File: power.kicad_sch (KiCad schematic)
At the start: 29 parts, among them CN104 Power, IC109 L7805, SW101 SW_SPDT

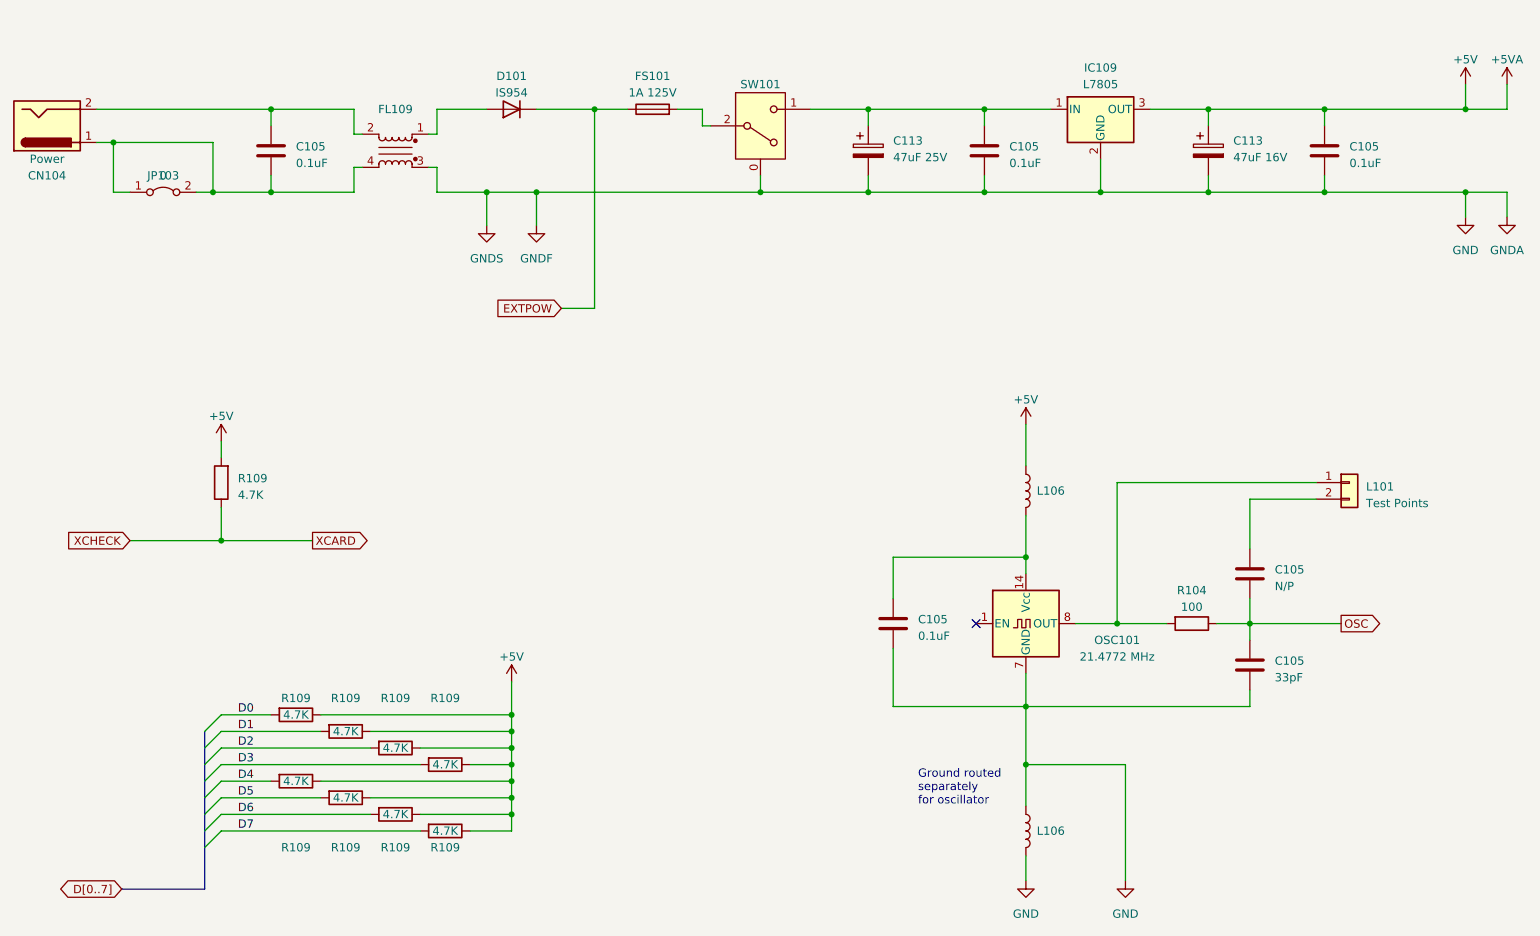
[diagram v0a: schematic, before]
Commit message: Inductor symbol for L101, schematic layout clean-up.
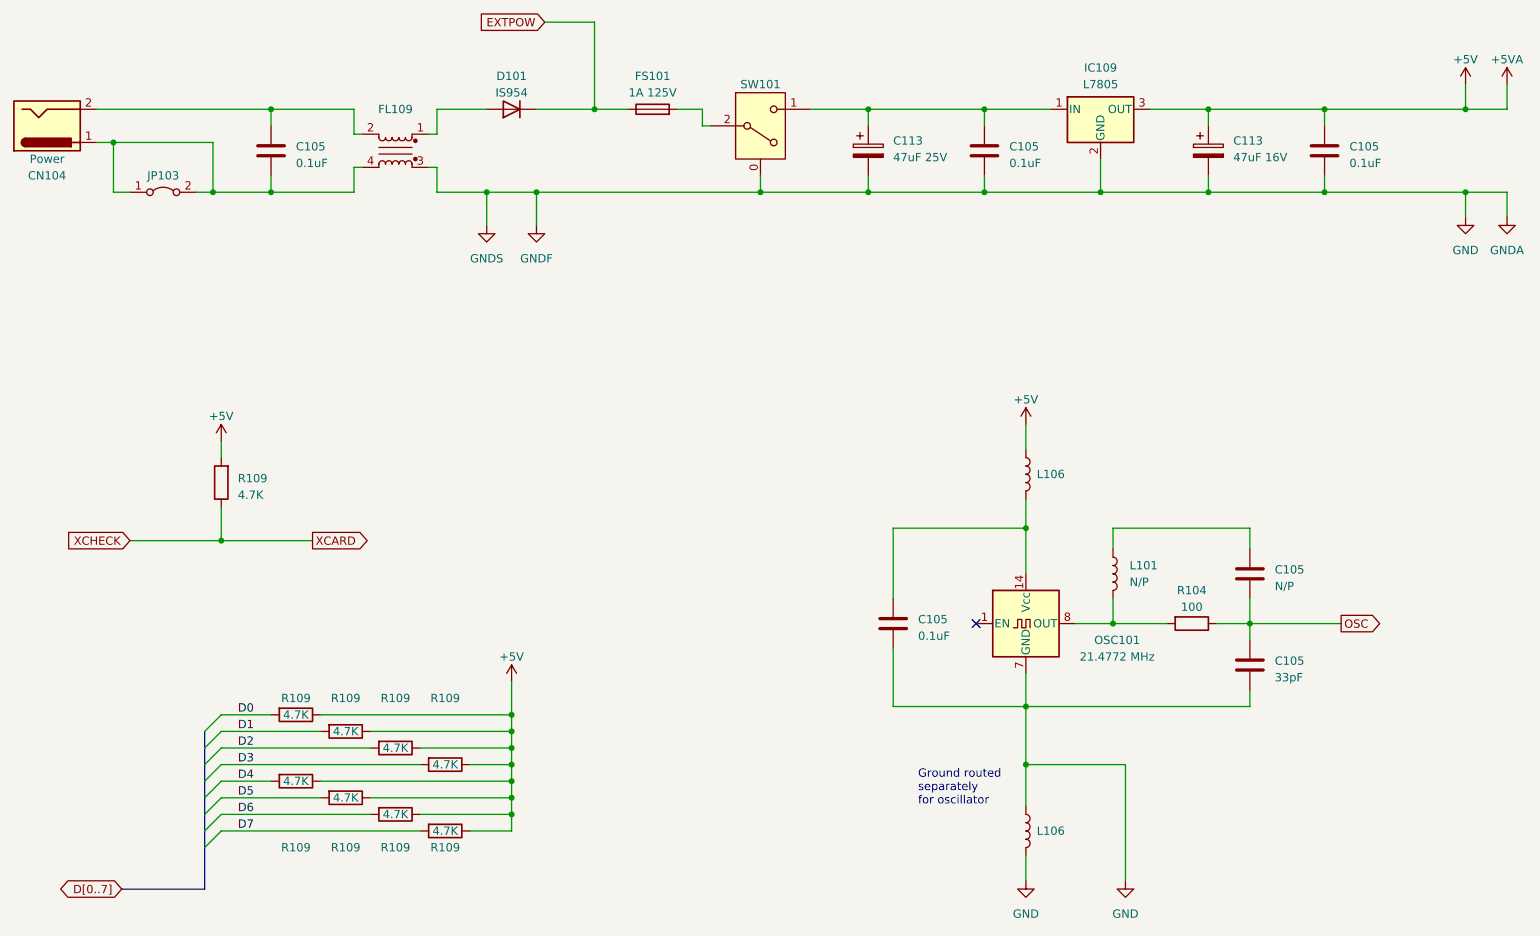
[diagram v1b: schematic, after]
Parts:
- L101: value Test Points -> N/P; symbol Connector_Generic:Conn_01x02 -> Device:L
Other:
- moved on the sheet: L106
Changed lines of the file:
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@@
   (title_block
     (title "PC Engine Power, Oscillator and Misc.")
-    (date "2023-09-18")
-    (rev "1.1")
+    (date "2023-09-20")
+    (rev "1.2")
     (comment 1 "Differences reverse engineered from original PWD-623A board")
     (comment 2 "Adapted from existing TurboGrafx-16 schematics by Cosam")
   )
-  (junction (at 255.27 129.54) (diameter 0) (color 0 0 0 0)
-  )
   (junction (at 308.61 50.8) (diameter 0) (color 0 0 0 0)
   )
@@
   (junction (at 252.73 63.5) (diameter 0) (color 0 0 0 0)
   )
-  (junction (at 241.3 119.38) (diameter 0) (color 0 0 0 0)
-  )
   (junction (at 118.11 116.84) (diameter 0) (color 0 0 0 0)
   )
@@
   (junction (at 162.56 143.51) (diameter 0) (color 0 0 0 0)
   )
+  (junction (at 254.635 129.54) (diameter 0) (color 0 0 0 0)
+  )
   (junction (at 241.3 151.13) (diameter 0) (color 0 0 0 0)
   )
   (junction (at 287.02 50.8) (diameter 0) (color 0 0 0 0)
+  )
+  (junction (at 241.3 114.935) (diameter 0) (color 0 0 0 0)
   )
   (junction (at 217.17 50.8) (diameter 0) (color 0 0 0 0)
@@
     (stroke (width 0) (type default))
   )
-  (wire (pts (xy 241.3 119.38) (xy 241.3 121.92))
-    (stroke (width 0) (type default))
-  )
   (wire (pts (xy 166.37 63.5) (xy 166.37 68.58))
     (stroke (width 0) (type default))
@@
     (stroke (width 0) (type default))
   )
+  (wire (pts (xy 254.635 114.935) (xy 254.635 118.11))
+    (stroke (width 0) (type default))
+  )
   (wire (pts (xy 151.13 50.8) (xy 158.75 50.8))
     (stroke (width 0) (type default))
@@
     (stroke (width 0) (type default))
   )
-  (wire (pts (xy 275.59 110.49) (xy 275.59 118.11))
+  (wire (pts (xy 275.59 114.935) (xy 275.59 118.11))
     (stroke (width 0) (type default))
   )
@@
     (stroke (width 0) (type default))
   )
-  (wire (pts (xy 285.75 107.95) (xy 255.27 107.95))
-    (stroke (width 0) (type default))
-  )
-  (wire (pts (xy 248.92 129.54) (xy 255.27 129.54))
+  (wire (pts (xy 248.92 129.54) (xy 254.635 129.54))
     (stroke (width 0) (type default))
   )
@@
     (stroke (width 0) (type default))
   )
-  (wire (pts (xy 220.98 119.38) (xy 220.98 125.73))
+  (wire (pts (xy 220.98 114.935) (xy 220.98 125.73))
     (stroke (width 0) (type default))
   )
@@
     (stroke (width 0) (type default))
   )
-  (wire (pts (xy 241.3 99.06) (xy 241.3 105.41))
+  (wire (pts (xy 241.3 99.06) (xy 241.3 102.87))
     (stroke (width 0) (type default))
   )
@@
     (stroke (width 0) (type default))
   )
+  (wire (pts (xy 275.59 114.935) (xy 254.635 114.935))
+    (stroke (width 0) (type default))
+  )
   (wire (pts (xy 241.3 142.24) (xy 241.3 151.13))
     (stroke (width 0) (type default))
@@
     (stroke (width 0) (type default))
   )
+  (wire (pts (xy 254.635 129.54) (xy 262.89 129.54))
+    (stroke (width 0) (type default))
+  )
   (wire (pts (xy 308.61 50.8) (xy 314.96 50.8))
     (stroke (width 0) (type default))
@@
     (stroke (width 0) (type default))
   )
-  (wire (pts (xy 241.3 119.38) (xy 220.98 119.38))
-    (stroke (width 0) (type default))
-  )
   (wire (pts (xy 133.35 143.51) (xy 162.56 143.51))
     (stroke (width 0) (type default))
@@
     (stroke (width 0) (type default))
   )
-  (wire (pts (xy 175.26 81.28) (xy 170.18 81.28))
+  (wire (pts (xy 175.26 37.465) (xy 167.64 37.465))
     (stroke (width 0) (type default))
   )
@@
     (stroke (width 0) (type default))
   )
-  (wire (pts (xy 175.26 50.8) (xy 175.26 81.28))
+  (wire (pts (xy 175.26 37.465) (xy 175.26 50.8))
     (stroke (width 0) (type default))
   )
@@
     (stroke (width 0) (type default))
   )
+  (wire (pts (xy 241.3 114.935) (xy 241.3 121.92))
+    (stroke (width 0) (type default))
+  )
   (wire (pts (xy 308.61 63.5) (xy 314.96 63.5))
     (stroke (width 0) (type default))
@@
     (stroke (width 0) (type default))
   )
+  (wire (pts (xy 241.3 114.935) (xy 220.98 114.935))
+    (stroke (width 0) (type default))
+  )
   (wire (pts (xy 314.96 63.5) (xy 314.96 67.31))
     (stroke (width 0) (type default))
@@
     (stroke (width 0) (type default))
   )
-  (wire (pts (xy 255.27 107.95) (xy 255.27 129.54))
-    (stroke (width 0) (type default))
-  )
-  (wire (pts (xy 285.75 110.49) (xy 275.59 110.49))
+  (wire (pts (xy 254.635 125.73) (xy 254.635 129.54))
     (stroke (width 0) (type default))
   )
@@
     (stroke (width 0) (type default))
   )
-  (wire (pts (xy 241.3 113.03) (xy 241.3 119.38))
-    (stroke (width 0) (type default))
-  )
-  (wire (pts (xy 255.27 129.54) (xy 262.89 129.54))
+  (wire (pts (xy 241.3 110.49) (xy 241.3 114.935))
     (stroke (width 0) (type default))
   )
@@
     )
   )
-  (global_label "EXTPOW" (shape input) (at 170.18 81.28 180) (fields_autoplaced)
+  (global_label "EXTPOW" (shape input) (at 167.64 37.465 180) (fields_autoplaced)
     (effects (font (size 1.27 1.27)) (justify right))
-    (property "Intersheetrefs" "${INTERSHEET_REFS}" (at 159.8962 81.28 0)
+    (property "Intersheetrefs" "${INTERSHEET_REFS}" (at 157.3562 37.465 0)
       (effects (font (size 1.27 1.27)) (justify right) hide)
     )
@@
     )
     (property "Value" "0" (at 109.22 60.96 0)
-      (effects (font (size 1.27 1.27)))
+      (effects (font (size 1.27 1.27)) hide)
     )
     (property "Footprint" "A-PCENGINE:Jumper_Link" (at 109.22 63.5 0)
@@
     )
   )
-  (symbol (lib_id "Connector_Generic:Conn_01x02") (at 290.83 107.95 0) (unit 1)
-    (in_bom yes) (on_board yes) (dnp no) (fields_autoplaced)
-    (property "Reference" "L101" (at 293.37 108.585 0)
+  (symbol (lib_id "Device:L") (at 254.635 121.92 0) (mirror x) (unit 1)
+    (in_bom yes) (on_board yes) (dnp no)
+    (property "Reference" "L101" (at 257.175 120.65 0)
       (effects (font (size 1.27 1.27)) (justify left))
     )
-    (property "Value" "Test Points" (at 293.37 111.125 0)
+    (property "Value" "N/P" (at 257.175 123.19 0)
       (effects (font (size 1.27 1.27)) (justify left))
     )
-    (property "Footprint" "A-PCENGINE:2xTest_Point" (at 290.83 107.95 0)
-      (effects (font (size 1.27 1.27)) hide)
-    )
-    (property "Datasheet" "~" (at 290.83 107.95 0)
+    (property "Footprint" "A-PCENGINE:2xTest_Point" (at 254.635 121.92 0)
+      (effects (font (size 1.27 1.27)) hide)
+    )
+    (property "Datasheet" "~" (at 254.635 121.92 0)
       (effects (font (size 1.27 1.27)) hide)
     )
@@
     )
   )
-  (symbol (lib_id "Device:L") (at 241.3 109.22 0) (unit 1)
-    (in_bom yes) (on_board yes) (dnp no)
-    (property "Reference" "L106" (at 245.11 109.22 0)
-      (effects (font (size 1.27 1.27)))
-    )
-    (property "Value" "~" (at 242.57 109.22 90)
-      (effects (font (size 1.27 1.27)))
-    )
-    (property "Footprint" "A-PCENGINE:L-5.00mm_Small_Silk" (at 241.3 109.22 0)
-      (effects (font (size 1.27 1.27)) hide)
-    )
-    (property "Datasheet" "~" (at 241.3 109.22 0)
-      (effects (font (size 1.27 1.27)) hide)
-    )
+  (symbol (lib_id "Device:L") (at 241.3 106.68 0) (unit 1)
+    (in_bom yes) (on_board yes) (dnp no)
+    (property "Reference" "L106" (at 245.11 106.68 0)
+      (effects (font (size 1.27 1.27)))
+    )
+    (property "Value" "~" (at 242.57 106.68 90)
+      (effects (font (size 1.27 1.27)))
+    )
+    (property "Footprint" "A-PCENGINE:L-5.00mm_Small_Silk" (at 241.3 106.68 0)
+      (effects (font (size 1.27 1.27)) hide)
+    )
+    (property "Datasheet" "~" (at 241.3 106.68 0)
+      (effects (font (size 1.27 1.27)) hide)
+    )

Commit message: Add contact info the schematics for publishing.
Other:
- company: (none) -> By Cosam
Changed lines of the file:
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@@
   (title_block
     (title "PC Engine Power, Oscillator and Misc.")
-    (date "2023-09-20")
-    (rev "1.2")
-    (comment 1 "Differences reverse engineered from original PWD-623A board")
-    (comment 2 "Adapted from existing TurboGrafx-16 schematics by Cosam")
+    (date "2023-11-15")
+    (rev "1.2.1")
+    (company "By Cosam")
+    (comment 1 "https://github.com/Board-Folk/PC-Engine")
+    (comment 2 "For contributions or corrections please visit:")
+    (comment 3 "Differences reverse engineered from original PWD-623A board")
+    (comment 4 "Adapted from existing TurboGrafx-16 schematics")
   )
   (junction (at 308.61 50.8) (diameter 0) (color 0 0 0 0)
